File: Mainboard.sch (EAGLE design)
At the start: 159 parts, among them IC1 LM234Z, J1 1981584-1, J2 POWER_JACKPTH_LOCK, Q1 IRLML5103, Q2 IRLML5103, Q3 IRLML5103, Q4 IRLML5103, Q5 IRLML5103, T1 NDS352A, T2 NDS352A, T3 NDS352A, T4 NDS352A, T5 NDS352A, U1 RFM23BP, U10 EP2W+, U11 S1216V8, U12 Value, U2 LSM9DS1, U3 MAX708RESA-T, U4 ATSAMD21G-A, U5 MAX4372TEUK+T, U6 MAX4372TEUK+T, U7 TPS54226PWPRPWP14_2P31X2P46-L, U8 LTC4121-4.2, U9 LC05111C13MTTTG, X1 BU-SMA-V, X2 BU-SMA-V, X3 BU-SMA-V, Y1 32.768kHz

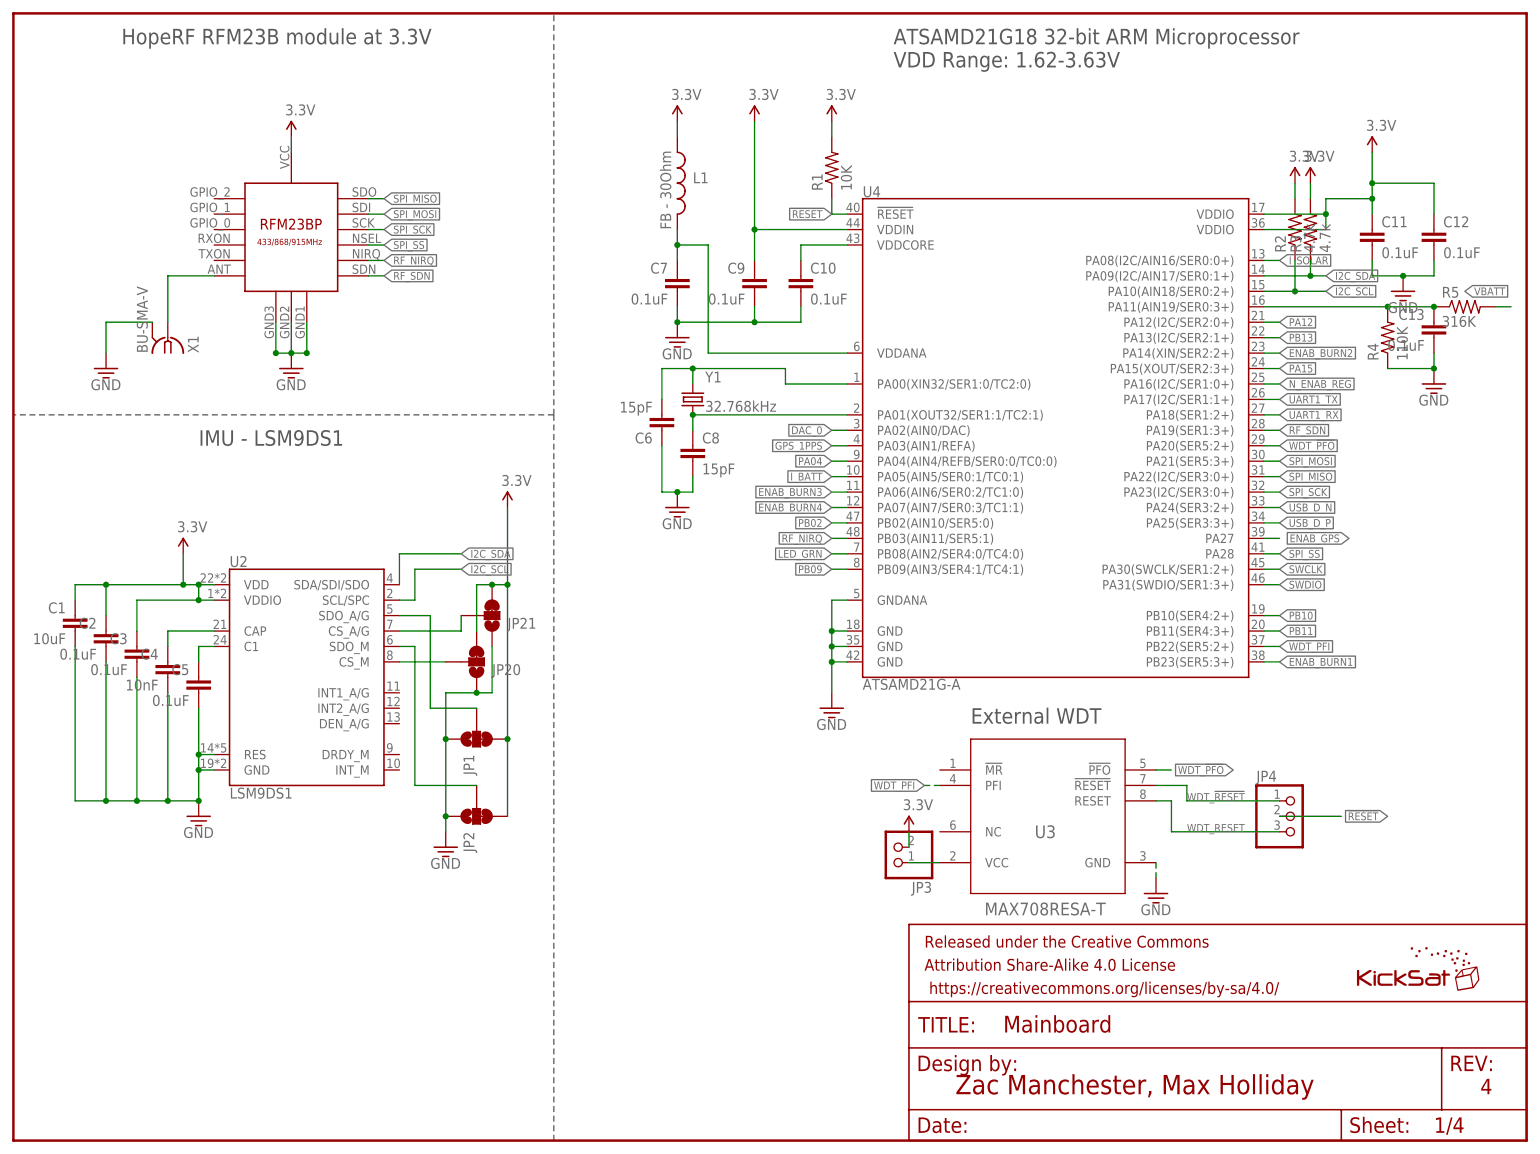
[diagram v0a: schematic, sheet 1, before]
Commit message: Latest kicksat2 mainboard update (KMB-21). New from KMB-20: MRAM, power relays, microSD card, 2 spots for [XLab Tester Boards](https://github.com/maholli/XTB)
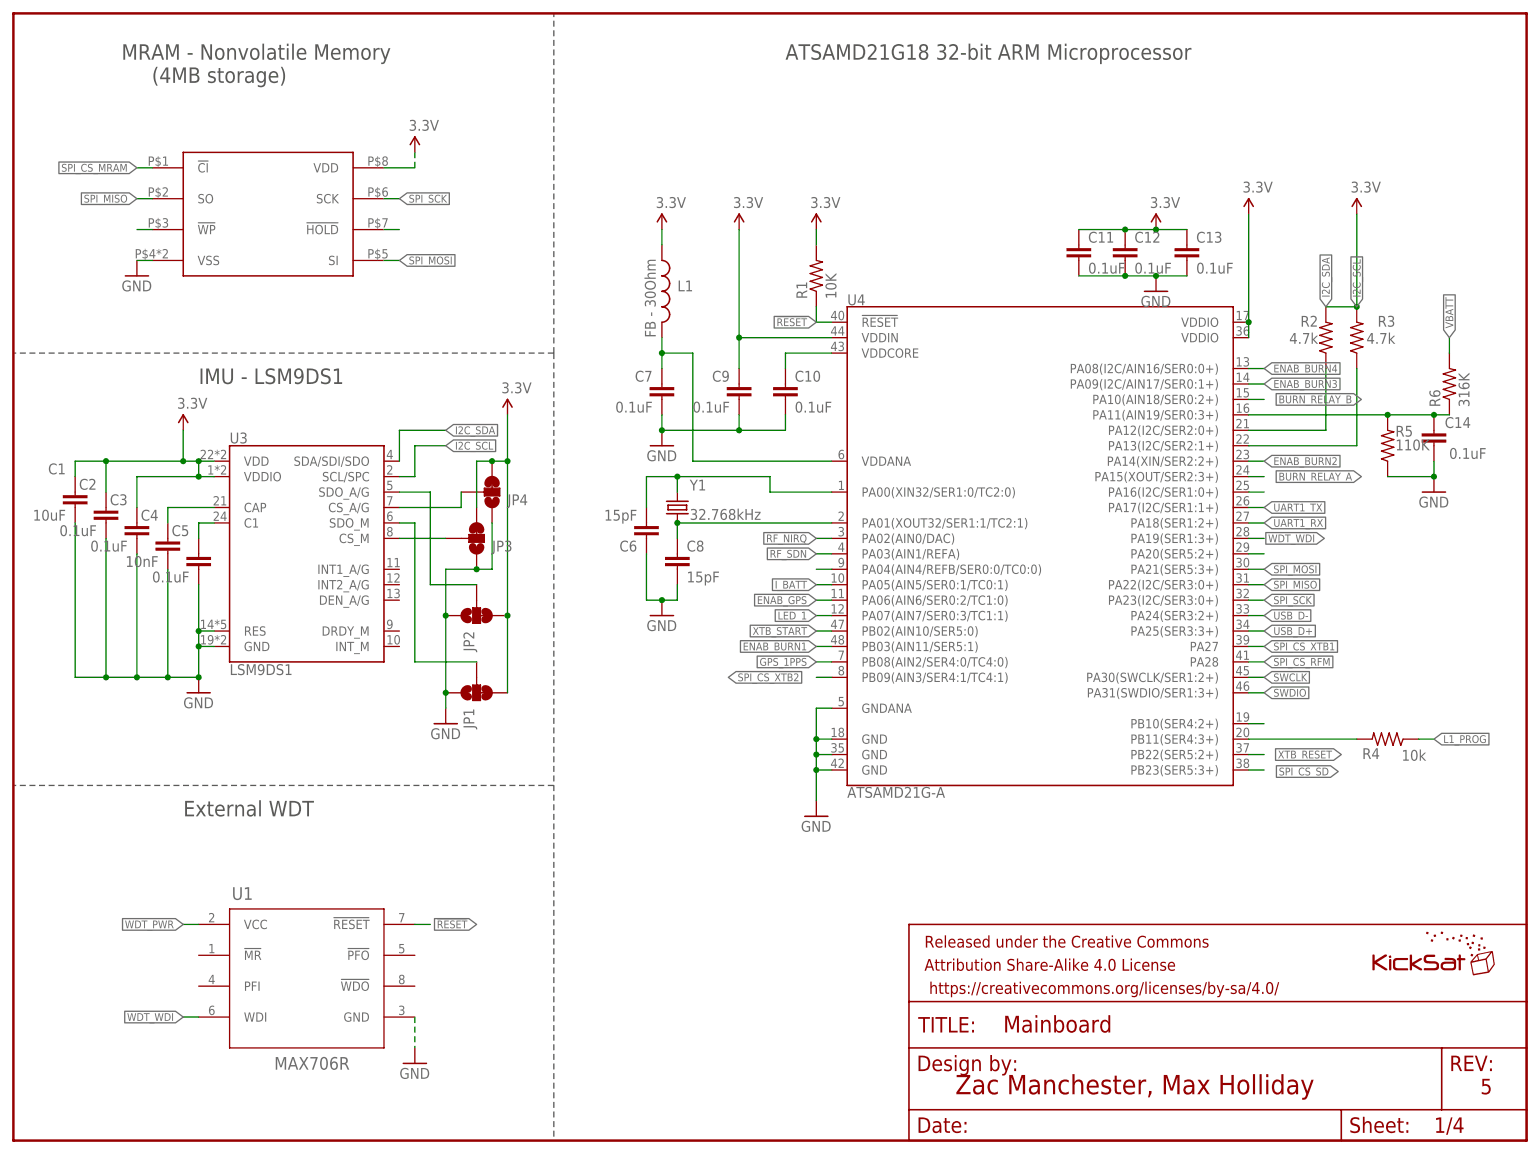
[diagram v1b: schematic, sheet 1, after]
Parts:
- removed C28: 0.1uF, SparkFun-Capacitors:0.1UF-0603-25V-5%
- removed C29, C30, C31, C32: .1uF, SparkFun-Capacitors:CAP0603-CAP
- removed C33: 2.2uF, SparkFun-Capacitors:2.2UF-0603-10V-20%
- removed C34: 0.33µF, SparkFun-Capacitors:0.33UF/330NF-0805-50V-10%
- removed C36: 10uF, SparkFun-Capacitors:10UF-0603-6.3V-20%
- removed D3: 200mA/70V, SparkFun-DiscreteSemi:BAV99
- removed IC1: LM234Z, linear:LM234Z
- removed JP18: M023.5MM_LOCK, SparkFun-Connectors:M023.5MM_LOCK
- removed JP19, JP20, JP21: JUMPER-PAD-3-2OF3_NC_BY_TRACE_SMALL, SparkFun-Passives:JUMPER-PAD-3-2OF3_NC_BY_TRACE_SMALL
- removed JP22, JP28: (no value), pinhead:PINHD-1X1
- removed JP7: (no value), SparkFun-Connectors:M03POLAR_LOCK
- removed R36, R37, R38: 10k, SparkFun-Resistors:RESISTOR0603
- removed R39, R40, R41, R42: 3.3k, SparkFun-Resistors:RESISTOR0603
- removed R43, R45: 330, SparkFun-Resistors:330OHM1/10W1%(0603)
- removed R44, R46, R47, R48, R49, R50, R51, R52, R53, R54, R55: 10K, SparkFun-Resistors:10KOHM-1/10W-1%(0603)0603
- removed R7: (no value), SparkFun-Resistors:RESISTOR0603
- removed T1, T2, T3, T4, T5: NDS352A, zetex:PMOSSOT23
- added 3.3V: (no value), pinhead:PINHD-1X1
- added J3: DCJ0303, maholli:DCJ0303
- added Q10, Q11, Q12, Q9: IRLML5103, User-Submitted:MOSFET-PCHANNEL
- added Q6, Q7, Q8: IRLML2803, maholli:IRLML2803TRPBF
- added U13: RFM23BP, RFM23BP:RFM23BP
- added U14: S1216V8, maholli:S1216V8
- C14: value 22uF -> 0.1uF; device SparkFun-Capacitors:22UF-0805-6.3V-20% -> SparkFun-Capacitors:0.1UF-25V(+80/-20%)(0603)
- C16: value 10uF -> 22uF; device SparkFun-Capacitors:10UF-0603-6.3V-20% -> SparkFun-Capacitors:22UF-0805-6.3V-20%
- C18: value 1.0uF -> 10uF; device SparkFun-Capacitors:1.0UF-0603-16V-10% -> SparkFun-Capacitors:10UF-0603-6.3V-20%
- C19: value 10uF -> 2.2uF; device SparkFun-Capacitors:10UF-0603-6.3V-20% -> SparkFun-Capacitors:2.2UF-0603-10V-20%
- C20: value 2.2uF -> 2.2nF; device SparkFun-Capacitors:2.2UF-0603-10V-20% -> SparkFun-Capacitors:2.2NF/2200PF-0603-50V-10%
- C21: value 2.2nF -> 10uF; device SparkFun-Capacitors:2.2NF/2200PF-0603-50V-10% -> SparkFun-Capacitors:10UF-0603-6.3V-20%
- C22: value .1uF -> 0.1uF; device SparkFun-Capacitors:CAP0603-CAP -> SparkFun-Capacitors:1.0UF-0603-16V-10%
- C23: value 0.1uF -> .1uF; device SparkFun-Capacitors:0.1UF-0603-25V-5% -> SparkFun-Capacitors:CAP0603-CAP
- C24: value 3.3nF -> 22uF; device SparkFun-Capacitors:3.3NF-0603-100V-10% -> SparkFun-Capacitors:0.1UF-0603-25V-5%
- C25: value 1.0uF -> 3.3nF; device SparkFun-Capacitors:1.0UF-0603-16V-10% -> SparkFun-Capacitors:3.3NF-0603-100V-10%
- C26: value 22uF -> 1.0uF; device SparkFun-Capacitors:0.1UF-0603-25V-5% -> SparkFun-Capacitors:1.0UF-0603-16V-10%
- C27: value 0.1uF -> 2.2uF; device SparkFun-Capacitors:0.1UF-0603-25V-5% -> SparkFun-Capacitors:2.2UF-0603-10V-20%
- J1: value 1981584-1 -> 503182-1852; device audio amplifier example:1981584-1 -> maholli:503182-1852
- J2: value POWER_JACKPTH_LOCK -> 10118194-0001LF; device SparkFun-Connectors:POWER_JACKPTH_LOCK -> 10118194-0001LF:10118194-0001LF
- JP10, JP13: value (none) -> M023.5MM_LOCK; device SparkFun-Connectors:M03POLAR_LOCK -> SparkFun-Connectors:M023.5MM_LOCK
- JP15: value M023.5MM_LOCK -> (none); device SparkFun-Connectors:M023.5MM_LOCK -> SparkFun-Connectors:M03POLAR_LOCK
- JP24: value (none) -> JUMPER-PAD-3-2OF3_NC_BY_TRACE_SMALL; device pinhead:PINHD-1X1 -> SparkFun-Passives:JUMPER-PAD-3-2OF3_NC_BY_TRACE_SMALL
- JP3: value (none) -> JUMPER-PAD-3-2OF3_NC_BY_TRACE_SMALL; device pinhead:PINHD-1X2 -> SparkFun-Passives:JUMPER-PAD-3-2OF3_NC_BY_TRACE_SMALL
- JP4: value (none) -> JUMPER-PAD-3-2OF3_NC_BY_TRACE_SMALL; device pinhead:PINHD-1X3 -> SparkFun-Passives:JUMPER-PAD-3-2OF3_NC_BY_TRACE_SMALL
- JP5: device pinhead:PINHD-1X6 -> SparkFun-Connectors:M03POLAR_LOCK
- JP8: device pinhead:PINHD-1X3 -> SparkFun-Connectors:M03POLAR_LOCK
- Q1, Q2, Q3, Q5: value IRLML5103 -> IRLML2803; device User-Submitted:MOSFET-PCHANNEL -> maholli:IRLML2803TRPBF
- R13: value 22.1 -> 470k
- R14: value 100K -> 22.1k
- R15: value 470k -> 4.7k
- R16: value 4.7k -> 6.04K
- R17: value 6.04K -> 100K
- R18: value 4.7K -> 10K
- R19: value 680 -> 4.7K
- R20: value 10K -> 3.3K
- R21: value 3.3K -> 10k; device resistor:R-US_R0603 -> SparkFun-Resistors:RESISTOR0603
- R22: value 1k -> 10k; device resistor:R-US_R0603 -> SparkFun-Resistors:RESISTOR0603
- R23, R24: value 4 -> 10k; device resistor:R-US_R0603 -> SparkFun-Resistors:RESISTOR0603
- R26, R27: value 4 -> 4.7k; device resistor:R-US_R0603 -> SparkFun-Resistors:RESISTOR0603
- R29, R30, R32: value 4 -> 100k; device resistor:R-US_R0603 -> SparkFun-Resistors:RESISTOR0603
- R31: value 4.7k -> 100k
- R33: value 4 -> 330; device resistor:R-US_R0603 -> SparkFun-Resistors:330OHM1/10W1%(0603)
- R34: value 4.7k -> 10K; device SparkFun-Resistors:RESISTOR0603 -> SparkFun-Resistors:10KOHM-1/10W-1%(0603)0603
- R35: value 10k -> 0.025; device SparkFun-Resistors:RESISTOR0603 -> resistor:R-US_R2512
- R4: value 110K -> 10k
- R5: value 316K -> 110K
- R6: value (none) -> 316K; device SparkFun-Resistors:RESISTOR0603 -> SparkFun-Resistors:10KOHM-1/10W-1%(0603)0603
- U1: value RFM23BP -> MAX706R; device RFM23BP:RFM23BP -> maholli:MAX708RESA-T; SPICEPREFIX U -> (none)
- U10: value EP2W+ -> XTB_2018_04_25; device maholli:EP2W+ -> maholli:XTB_2018_04_25
- U11: value S1216V8 -> XTB_2018_04_25; device maholli:S1216V8 -> maholli:XTB_2018_04_25
- U12: value Value -> EP2W+; device maholli:ADS124S08IPBSR -> maholli:EP2W+
- U2: value LSM9DS1 -> MR25H40; device SparkFun-Sensors:LSM9DS1 -> maholli:MR25H40
- U3: value MAX708RESA-T -> LSM9DS1; device maholli:MAX708RESA-T -> SparkFun-Sensors:LSM9DS1
- U6: value MAX4372TEUK+T -> LTC4121-4.2; device maholli:MAX4372TEUK+T -> BrownSpaceEngineering:LTC4121-4.2
- U8: value LTC4121-4.2 -> PE014006; device BrownSpaceEngineering:LTC4121-4.2 -> maholli:PE014005
- U9: value LC05111C13MTTTG -> PE014006; device BrownSpaceEngineering:LC05111C13MTTTG -> maholli:PE014005
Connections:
- net PA04 renamed N$22
- removed net 3.3V_REF: U12.REFP0
- removed net A_3.3V: U12.AVDD
- removed net DAC_0: JP22.1, U4.PA02(AIN0/DAC)
- removed net GPS_PWR: Q1.S, U11.VCC
- removed net I_SOLAR: U4.PA08(I2C/AIN16/SER0:0+), U6.OUT
- removed net LED_GRN: D2.C, U4.PB08(AIN2/SER4:0/TC4:0)
- removed net N$22 (its old number): J2.GND, J2.GNDBREAK, JP11.2, JP12.2, JP15.1
- removed net N$27: R48.1, U12.AIN1
- removed net N$41: C27.1, R19.1, U9.VCC
- removed net N$42: C17.1, U7.VCC
- removed net N$45: R22.2, U9.CS
- removed net N$48: R51.1, U12.AIN4
- removed net N$50: R46.1, U12.GPIO0_AIN8
- removed net N$56: R55.1, U12.GPIO3_AIN11
- removed net N_ENAB_REG: U4.PA16(I2C/SER1:0+), U7.EN
- removed net PA12: JP24.1, U4.PA12(I2C/SER2:0+)
- removed net PA15: U4.PA15(XOUT/SER2:3+)
- removed net PB02: JP28.1, U4.PB02(AIN10/SER5:0)
- removed net PB09: JP27.1, U4.PB09(AIN3/SER4:1/TC4:1)
- removed net PB10: JP26.1, U4.PB10(SER4:2+)
- removed net PB11: JP25.1, U4.PB11(SER4:3+)
- removed net PB13: U4.PA13(I2C/SER2:1+)
- removed net PWR_GND: C14.1, C15.1, C16.2, C17.2, C24.2, C25.2, R13.1, U7.EPAD, U7.GND, U7.PGND1, U7.PGND2
- removed net SPI_SS: U1.NSEL, U4.PA28
- removed net SPI_SS2: U12.CS_N
- removed net USB_D_N: J1.D-, U4.PA24(SER3:2+)
- removed net USB_D_P: J1.D+, U4.PA25(SER3:3+)
- removed net USB_ID: J1.ID, JP8.2
- removed net VBURN_IN: Q2.D, Q3.D, Q4.D, Q5.D, R23.1, R24.1, R26.1, R27.1, R29.1, R30.1, R32.1, R33.1, R39.2, R40.2, R41.2, R42.2
- removed net WDT_!PFO: U3.!PFO, U4.PA20(SER5:2+)
- removed net WDT_!RESET: JP4.1, U3.!RESET
- removed net WDT_PFI: U3.PFI, U4.PB22(SER5:2+)
- removed net WDT_RESET: JP4.3, U3.RESET
- new net BURN_RELAY_A: Q2.G, U4.PA15(XOUT/SER2:3+)
- new net BURN_RELAY_B: Q1.G, U4.PA10(AIN18/SER0:2+)
- new net GPS_PWR_IN: Q4.D, R34.2, U14.VCC, U14.V_BCKP
- new net LED_1: D2.C, U4.PA07(AIN7/SER0:3/TC1:1)
- new net SPI_CS_MRAM: U2.!CI
- new net SPI_CS_RFM: U13.NSEL, U4.PA28
- new net SPI_CS_SD: J1.CD/DAT3, U4.PB23(SER5:3+)
- new net SPI_CS_XTB1: U10.SPI_CS, U4.PA27
- new net SPI_CS_XTB2: U11.SPI_CS, U4.PB09(AIN3/SER4:1/TC4:1)
- new net USB_D+: J2.D+, U4.PA25(SER3:3+)
- new net USB_D-: J2.D-, U4.PA24(SER3:2+)
- new net VBATT_IN: C27.1, F2.2, JP10.1, JP11.1, JP13.2
- new net VBURN_A_IN: Q12.S, Q9.S, R31.2, R32.2, U9.11
- new net VBURN_B_IN: Q10.S, Q11.S, R29.2, R30.2, U8.11
- new net WDT_PWR: U1.VCC
- new net WDT_WDI: U1.WDI, U4.PA19(SER1:3+)
- new net XTB_RESET: U10.RESET, U11.RESET, U4.PB22(SER5:2+)
- new net XTB_START: U10.START, U11.START, U4.PB02(AIN10/SER5:0)
- net !RESET: now also JP27.1, U1.!RESET; no longer JP4.2, JP5.3
- net 3.3V: now also 3.3V.1, C13.1, C16.2, J1.VDD, JP3.3, JP4.3, Q4.S, R13.2, R20.1, U10.AVDD, U10.DVDD, U10.HALL_PWR, U10.INA_VDD, U11.AVDD, U11.DVDD, U11.HALL_PWR, U11.INA_VDD, U13.VCC, U3.VDD, U3.VDDIO; no longer C14.2, C22.1, JP20.3, JP21.3, JP3.2, JP5.2, JP8.1, Q1.D, R16.2, R21.1, R23.2, R24.2, R26.2, R27.2, R29.2, R30.2, R32.2, R43.2, R44.2, R7.1, U1.VCC, U11.V_BCKP, U12.DVDD, U12.IOVDD, U2.VDD, U2.VDDIO, U6.RS-, U6.VCC
- net ENAB_BURN1: now also R24.1, U4.PB03(AIN11/SER5:1); no longer R35.1, U4.PB23(SER5:3+)
- net ENAB_BURN2: now also R23.1; no longer R36.1
- net ENAB_BURN3: now also R22.1, R27.2, U4.PA09(I2C/AIN17/SER0:1+); no longer R31.2, R37.1, U4.PA06(AIN6/SER0:2/TC1:0)
- net ENAB_BURN4: now also R21.1, R26.2, U4.PA08(I2C/AIN16/SER0:0+); no longer R34.2, R38.1, U4.PA07(AIN7/SER0:3/TC1:1)
- net ENAB_GPS: now also R19.1, U4.PA06(AIN6/SER0:2/TC1:0); no longer R20.2, U4.PA27
- net GND: now also C14.2, C15.1, C16.1, C17.2, C18.2, C21.2, C24.2, C25.2, J1.SHIELD, J1.VSS, J2.GND, JP12.2, JP15.1, JP24.1, JP3.1, JP4.1, JP8.1, Q3.S, Q5.S, Q6.S, Q7.S, Q8.S, R14.1, R16.1, R21.2, R22.2, R23.2, R24.2, R5.1, U1.GND, U11.GND, U12.GND, U13.GND, U14.GND@10, U14.GND@12, U14.GND@13, U14.GND@24, U2.VSS, U3.RES, U6.FREQ, U6.NC, U6.NTC, U7.EPAD, U7.GND, U7.PGND1, U7.PGND2, U8.12, U8.A2, U9.12, U9.A2; no longer C20.2, C22.2, C28.2, C29.2, C30.2, C31.2, C32.2, C33.2, C34.1, C34.2, C36.1, J1.GND, J1.S1, JP10.1, JP13.1, JP15.2, JP19.1, JP20.1, JP21.1, JP5.6, JP7.1, JP8.3, R17.1, R22.1, R25.1, R28.1, R31.1, R34.1, R4.1, T1.S, T2.S, T3.S, T4.S, T5.S, U1.GND1, U1.GND2, U1.GND3, U10.GND@1, U10.GND@10, U10.GND@11, U10.GND@12, U10.GND@13, U10.GND@14, U10.GND@16, U10.GND@17, U10.GND@18, U10.GND@19, U10.GND@2, U10.GND@20, U10.GND@21, U10.GND@22, U10.GND@23, U10.GND@24, U10.GND@25, U10.GND@27, U10.GND@28, U10.GND@29, U10.GND@3, U10.GND@30, U10.GND@31, U10.GND@32, U10.GND@5, U10.GND@6, U10.GND@7, U10.GND@8, U10.GND@9, U11.GND@10, U11.GND@12, U11.GND@13, U11.GND@24, U12.AVSS, U12.AVSS-SW, U12.CLK, U12.DGND, U12.REFCOM, U12.REFN0, U12.START_SYNC, U2.GND, U2.RES, U8.FREQ, U8.GND, U8.NC, U8.NTC, U9.S2, U9.TST, U9.VSS
- net GPS_1PPS: now also U14.1PPS, U4.PB08(AIN2/SER4:0/TC4:0); no longer U11.1PPS, U4.PA03(AIN1/REFA)
- net I2C_SCL: now also R3.1, U3.SCL/SPC, U4.PA13(I2C/SER2:1+); no longer R2.1, U11.SCL/NC, U2.SCL/SPC, U4.PA10(AIN18/SER0:2+)
- net I2C_SDA: now also R2.1, U3.SDA/SDI/SDO, U4.PA12(I2C/SER2:0+); no longer R3.1, U11.SDA/NC, U2.SDA/SDI/SDO, U4.PA09(I2C/AIN17/SER0:1+)
- net I2C_SDOA/G: now also JP2.2, U3.SDO_A/G; no longer JP1.2, U2.SDO_A/G
- net L1_CHG: now also U6.RUN; no longer U8.RUN
- net L1_FAULTN: now also R15.1, U6.~FAULT; no longer R16.1, U8.~FAULT
- net L1_PROG: now also R16.2, R4.1, U6.PROG; no longer R17.2, U8.PROG
- net LION1: now also C24.1, U6.BAT, U6.BATSNS; no longer C26.1, R19.2, U8.BAT, U8.BATSNS
- net N$1: now also R33.1; no longer R43.1
- net N$10: now also Q3.G, R19.2; no longer C28.1, R20.1, T1.G
- net N$11: now also Q5.G, R25.1; no longer C31.1, R37.2, T4.G
- net N$12: now also Q3.D, Q4.G, R20.2; no longer Q1.G, R21.2, T1.D
- net N$13: now also C14.1, R5.2, R6.1, U4.PA11(AIN19/SER0:3+); no longer F2.1, J1.VBUS
- net N$14: now also C22.2; no longer C18.2
- net N$15: now also Q12.G, Q8.D, R31.1; no longer Q3.G, R40.1, T3.D
- net N$16: now also U12.PORT1; no longer U10.PORT1
- net N$17: now also U12.PORT2, X1.1; no longer U10.PORT2, X3.1
- net N$19: now also U13.ANT, X3.1; no longer U1.ANT, X1.1
- net N$2: now also U3.CAP; no longer U2.CAP
- net N$20: now also F2.1, J2.VDD; no longer R47.1, U12.AIN0
- net N$21: now also JP1.2, U3.SDO_M; no longer JP2.2, U2.SDO_M
- net N$23: now also JP3.2, U3.CS_M; no longer JP20.2, U2.CS_M
- net N$24: now also JP24.3, R34.1; no longer JP19.3, R44.1
- net N$25: now also Q8.G, R28.1; no longer C29.1, R35.2, T2.G
- net N$26: now also JP4.2, U3.CS_A/G; no longer JP21.2, U2.CS_A/G
- net N$3: now also C22.1; no longer C18.1
- net N$30: now also Q7.G, R27.1; no longer R49.1, U12.AIN2
- net N$31: now also U2.!WP; no longer IC1.R, R45.2
- net N$32: now also C20.2, U6.SW; no longer C21.2, U8.SW
- net N$33: now also C20.1, U6.BOOST; no longer C21.1, U8.BOOST
- net N$34: now also C19.1, U6.INTVCC; no longer C20.1, U8.INTVCC
- net N$35: now also U6.MPPT; no longer U8.MPPT
- net N$36: now also U6.CHGSNS; no longer U8.CHGSNS
- net N$37: now also R13.1, U6.~CHRG; no longer R15.1, U8.~CHRG
- net N$38: now also Q2.S, U9.A1; no longer C32.1, R38.2, T5.G
- net N$39: now also U2.VDD; no longer D3.A1, IC1.V-, R45.1
- net N$4: now also JP13.1, JP16.2; no longer JP16.1, JP18.2
- net N$40: now also Q1.S, U8.A1; no longer C13.1, R4.2, R5.1, U4.PA11(AIN19/SER0:3+)
- net N$43: now also J3.2, J3.3, JP10.2, JP11.2, JP12.1; no longer R50.1, U12.AIN3
- net N$44: now also Q11.G, Q7.D, R30.1; no longer Q4.G, R41.1, T4.D
- net N$46: now also C26.1, R17.2; no longer C25.1, R14.2
- net N$47: now also Q10.G, Q6.D, R29.1; no longer Q5.G, R42.1, T5.D
- net N$49: now also U2.!HOLD; no longer R52.1, U12.AIN5
- net N$5: now also Q6.G, R26.1; no longer C30.1, R36.2, T3.G
- net N$51: now also C25.1; no longer C24.1
- net N$52: now also R14.2; no longer R13.2
- net N$53: now also U4.PA20(SER5:2+); no longer R53.1, U12.GPIO1_AIN9
- net N$54: now also U4.PA16(I2C/SER1:0+); no longer C36.2, U12.REFOUT
- net N$55: now also U4.PB10(SER4:2+); no longer R54.1, U12.GPIO2_AIN10
- net N$6: now also U3.C1; no longer U2.C1
- net N$7: now also Q5.D, Q9.G, R32.1; no longer Q2.G, R39.1, T2.D
- net N$8: now also R4.2, U4.PB11(SER4:3+); no longer JP3.1, U3.VCC
- net N$9: now also JP24.2, U14.RSTN; no longer JP19.2, U11.RSTN
- net PGOOD: now also R17.1; no longer R14.1
- net RF_IN: now also U12.SUM_PORT, U14.RF_IN; no longer U10.SUM_PORT, U11.RF_IN
- net RF_NIRQ: now also U13.NIRQ, U4.PA02(AIN0/DAC); no longer U1.NIRQ, U4.PB03(AIN11/SER5:1)
- net RF_SDN: now also U13.SDN, U4.PA03(AIN1/REFA); no longer U1.SDN, U4.PA19(SER1:3+)
- net SPI_MISO: now also J1.DAT0, U10.SPI_MISO, U11.SPI_MISO, U13.SDO, U2.SO; no longer U1.SDO, U12.DIN, U12.DOUT_DRDY_N
- net SPI_MOSI: now also J1.CMD, U10.SPI_MOSI, U11.SPI_MOSI, U13.SDI, U2.SI; no longer U1.SDI
- net SPI_SCK: now also J1.CLK, U10.SPI_SCK, U11.SPI_SCK, U13.SCK, U2.SCK; no longer U1.SCK, U12.SCLK
- net SWCLK: now also JP26.1; no longer JP5.4
- net SWDIO: now also JP25.1; no longer JP5.5
- net UART1_RX: now also U14.TXD; no longer U11.TXD
- net UART1_TX: now also U14.RXD; no longer U11.RXD
- net VBATT: now also J3.1, JP16.1, Q1.D, Q2.D, R35.2, U7.EN, U8.14, U9.14; no longer C33.1, F2.2, J2.PWR, JP11.1, JP12.1, JP16.2, JP18.1, R5.2
- net VBURN1: now also Q9.D; no longer Q2.S
- net VBURN2: now also JP5.3, Q12.D; no longer JP7.3, Q3.S
- net VBURN3: now also JP9.3, Q11.D; no longer JP10.3, Q4.S
- net VBURN4: now also JP8.3, Q10.D; no longer JP9.3, Q5.S
- net VREG_IN: now also C18.1, C21.1, R35.1, U7.VCC; no longer C16.1, R6.1
- net VSOLAR: now also JP15.2, JP5.2, JP9.2; no longer JP10.2, JP13.2, JP7.2, R7.2, U6.RS+
- net VSOLAR_IN: now also C17.1, U6.IN; no longer C19.1, U8.IN
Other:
- note added: "5"
- note added: "ATSAMD21G18 32-bit ARM Microprocessor"
- note added: "Antenna"
- note added: "Decide on HOLD and !WP"
- note added: "MRAM - Nonvolatile Memory (4MB storage)"
- note added: "MicroSD Card"
- note added: "Power Relays"
- note added: "RF Splitter (2 Way, 0deg DC-Pass)"
- note added: "Regulator - 3.3V OUT"
- note added: "Sprite deployment"
- note added: "To Do: Characterize power consumption Validate SPI pinout of SAMD21"
- note added: "VBATT 4.5 to 18V"
- note added: "Xlab Test Boards (XTB)"
- note removed: "4"
- note removed: "ATSAMD21G18 32-bit ARM Microprocessor VDD Range: 1.62-3.63V"
- note removed: "Buck Converter - 3.3V OUT"
- note removed: "Burn Wire 1"
- note removed: "Burn Wire 2"
- note removed: "Burn Wire 3"
- note removed: "Burn Wire 4"
- note removed: "FREQ tied to GND to select 750kHz switching frequency"
- note removed: "LTC4121 can handle several amps of inrush current upon battery connection"
- note removed: "NC tied to ground prevent charge buildup, approved by LT."
- note removed: "NTC tied to GND b/c no NTC sensor"
- note removed: "Pick Rsense 0.1%"
- note removed: "Place L1 near SW pin"
- note removed: "R28 & R29 set Vmp=9V"
- note removed: "RF Splitter - 2 Way, 0deg DC-Pass"
- note removed: "Run pulled up to ensure charging on startup"
- note removed: "Solar Panel Current Sensor"
- note removed: "To Do: XLab Mez board design Stretch Goals: Ultracap Power Supply Max GFET sensor"
- note removed: "Ven threshold is 2.45V. Resistor divider sets RUN high when Solar Panel Voltage is >=6V."
- moved on the sheet: C1, C10, C11, C12, C13, C15, C17, C18, C19, C2, C20, C21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
